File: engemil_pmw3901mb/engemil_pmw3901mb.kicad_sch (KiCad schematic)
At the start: 16 parts, among them J1 6130XX11121, U1 PMW3901MB-TXQT, U2 TLV77333PDBVR, U3 TLV77318PDBVR

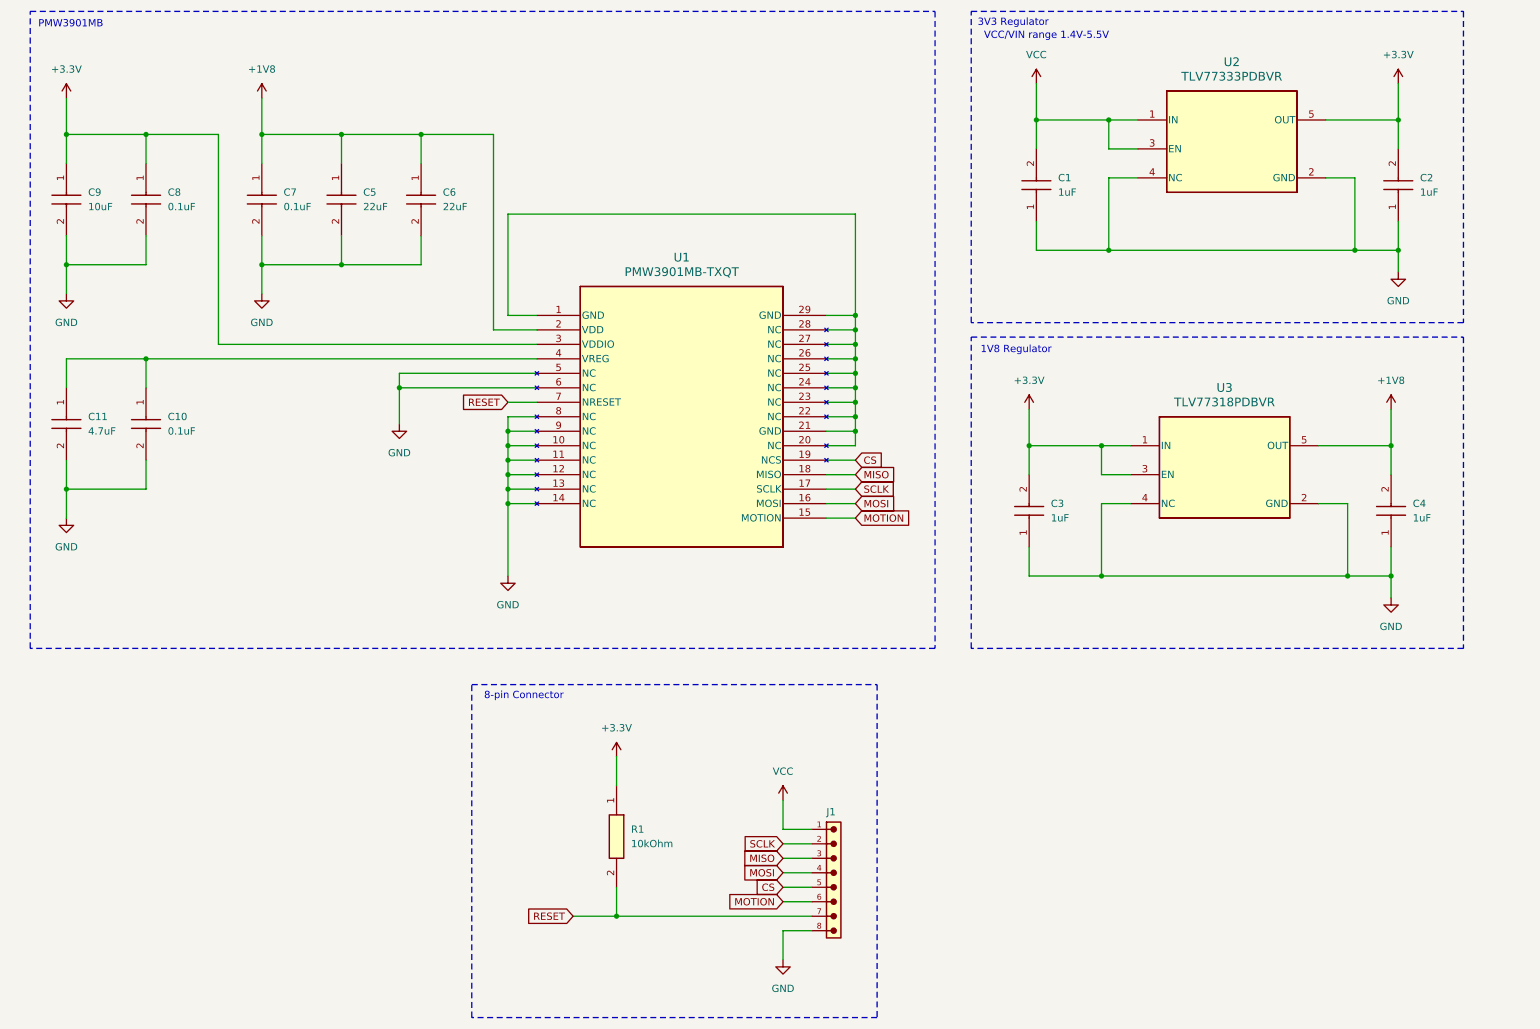
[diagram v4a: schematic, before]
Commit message: - Updated notes in schematic - Updated PMW3901MB NCS pin fron not connected to unspecified - Updated component orientation in PCB editor
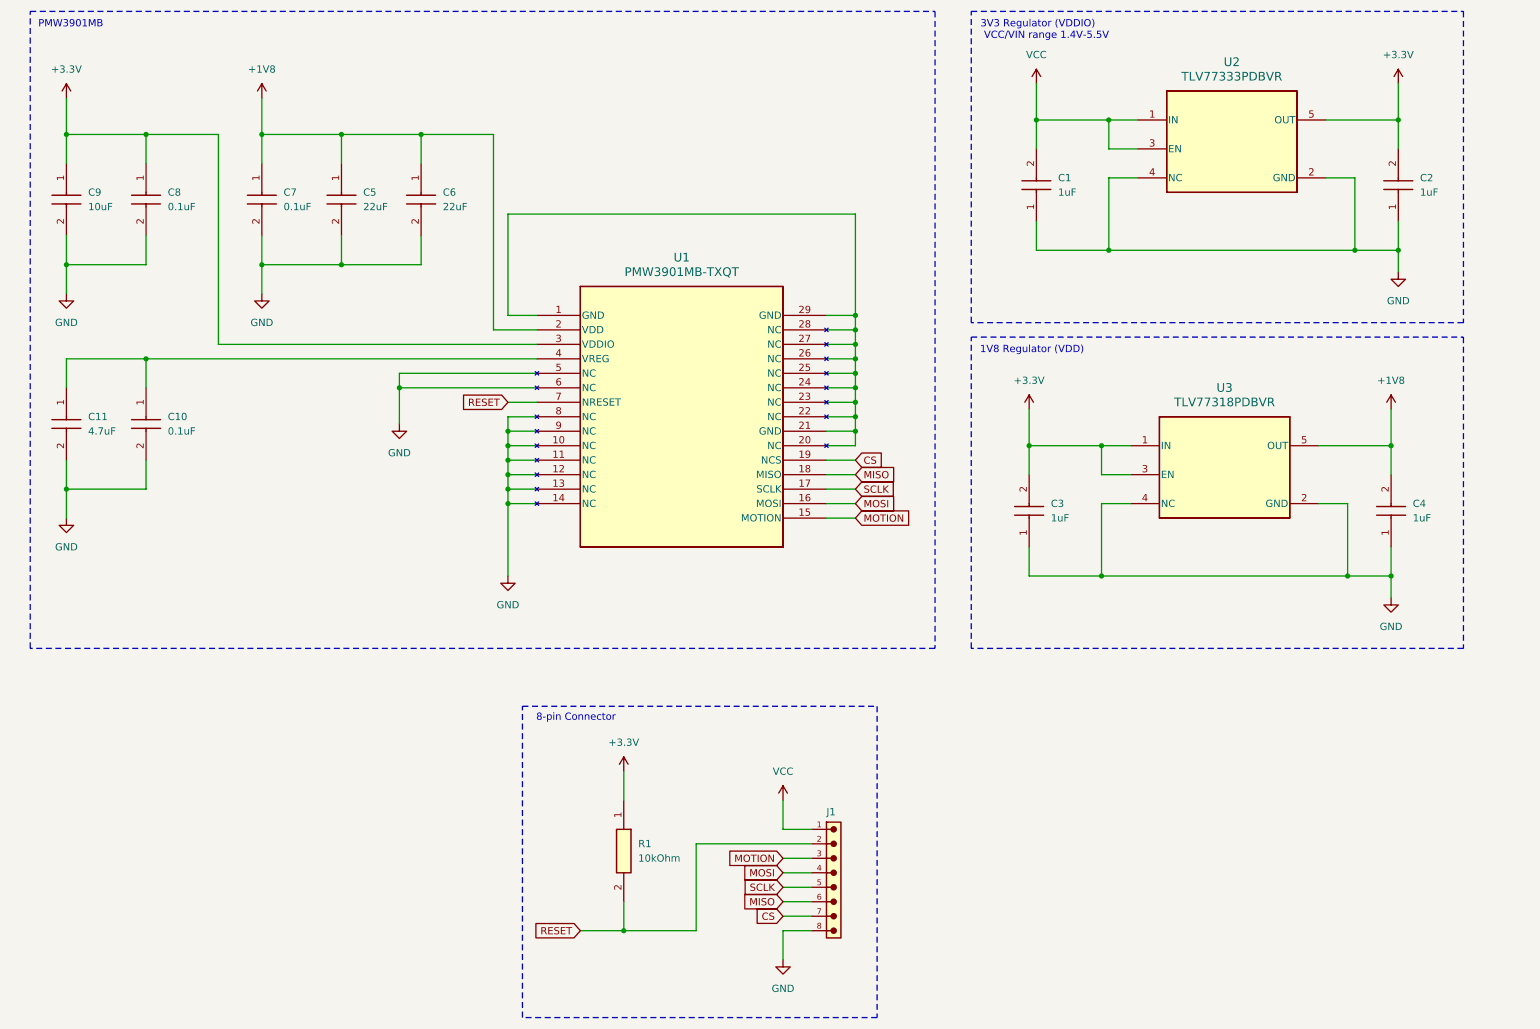
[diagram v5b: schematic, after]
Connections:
- net CS: now also J1.7; no longer J1.5
- net MISO: now also J1.6; no longer J1.3
- net MOTION: now also J1.3; no longer J1.6
- net RESET: now also J1.2; no longer J1.7
- net SCLK: now also J1.5; no longer J1.2
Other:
- note added: "1V8 Regulator (VDD)"
- note added: "3V3 Regulator (VDDIO)"
- note removed: "1V8 Regulator"
- note removed: "3V3 Regulator"
- moved on the sheet: R1
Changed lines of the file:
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@@
 	)
 	(rectangle
-		(start 95.25 134.62)
+		(start 104.14 138.43)
 		(end 166.37 193.04)
 		(stroke
@@
 	(text "8-pin Connector"
 		(exclude_from_sim no)
-		(at 104.394 136.652 0)
+		(at 113.538 140.462 0)
 		(effects
 			(font
@@
 		)
 	)
-	(text "3V3 Regulator"
+	(text "3V3 Regulator (VDDIO)"
 		(exclude_from_sim no)
-		(at 190.246 18.542 0)
+		(at 194.564 18.796 0)
 		(effects
 			(font
@@
 		)
 	)
-	(text "1V8 Regulator"
+	(text "1V8 Regulator (VDD)"
 		(exclude_from_sim no)
-		(at 190.754 75.946 0)
+		(at 193.548 75.946 0)
 		(effects
 			(font
@@
 	)
 	(junction
-		(at 120.65 175.26)
-		(diameter 0)
-		(color 0 0 0 0)
-	)
-	(junction
 		(at 193.04 92.71)
 		(diameter 0)
@@
 	)
 	(junction
+		(at 121.92 177.8)
+		(diameter 0)
+		(color 0 0 0 0)
+	)
+	(junction
 		(at 162.56 69.85)
 		(diameter 0)
@@
 	(wire
 		(pts
+			(xy 149.86 172.72) (xy 154.94 172.72)
+		)
+		(stroke
+			(width 0)
+			(type default)
+		)
+	)
+	(wire
+		(pts
 			(xy 205.74 115.57) (xy 193.04 115.57)
 		)
@@
 	(wire
 		(pts
-			(xy 243.84 102.87) (xy 248.92 102.87)
+			(xy 149.86 175.26) (xy 154.94 175.26)
 		)
 		(stroke
@@
 	(wire
 		(pts
-			(xy 149.86 172.72) (xy 154.94 172.72)
+			(xy 243.84 102.87) (xy 248.92 102.87)
 		)
 		(stroke
@@
 	(wire
 		(pts
-			(xy 149.86 170.18) (xy 154.94 170.18)
+			(xy 86.36 55.88) (xy 86.36 60.96)
 		)
 		(stroke
@@
 	(wire
 		(pts
-			(xy 86.36 55.88) (xy 86.36 60.96)
+			(xy 134.62 177.8) (xy 121.92 177.8)
 		)
 		(stroke
@@
 	(wire
 		(pts
-			(xy 120.65 175.26) (xy 154.94 175.26)
+			(xy 194.31 35.56) (xy 194.31 40.64)
 		)
 		(stroke
@@
 	(wire
 		(pts
-			(xy 194.31 35.56) (xy 194.31 40.64)
+			(xy 72.39 60.96) (xy 72.39 55.88)
 		)
 		(stroke
@@
 	(wire
 		(pts
-			(xy 72.39 60.96) (xy 72.39 55.88)
+			(xy 24.13 38.1) (xy 24.13 43.18)
 		)
 		(stroke
@@
 	(wire
 		(pts
-			(xy 24.13 38.1) (xy 24.13 43.18)
+			(xy 101.6 85.09) (xy 106.68 85.09)
 		)
 		(stroke
@@
 	(wire
 		(pts
-			(xy 101.6 85.09) (xy 106.68 85.09)
+			(xy 149.86 170.18) (xy 154.94 170.18)
 		)
 		(stroke
@@
 	(wire
 		(pts
-			(xy 162.56 82.55) (xy 162.56 85.09)
+			(xy 134.62 162.56) (xy 134.62 177.8)
 		)
 		(stroke
@@
 	(wire
 		(pts
-			(xy 257.81 58.42) (xy 257.81 62.23)
+			(xy 162.56 82.55) (xy 162.56 85.09)
 		)
 		(stroke
@@
 	(wire
 		(pts
-			(xy 212.09 40.64) (xy 207.01 40.64)
+			(xy 257.81 58.42) (xy 257.81 62.23)
 		)
 		(stroke
@@
 	(wire
 		(pts
-			(xy 149.86 162.56) (xy 154.94 162.56)
+			(xy 212.09 40.64) (xy 207.01 40.64)
 		)
 		(stroke
@@
 	(wire
 		(pts
-			(xy 113.03 175.26) (xy 120.65 175.26)
+			(xy 114.3 177.8) (xy 121.92 177.8)
+		)
+		(stroke
+			(width 0)
+			(type default)
+		)
+	)
+	(wire
+		(pts
+			(xy 154.94 162.56) (xy 134.62 162.56)
 		)
 		(stroke
@@
 	(wire
 		(pts
-			(xy 120.65 170.18) (xy 120.65 175.26)
+			(xy 121.92 172.72) (xy 121.92 177.8)
 		)
 		(stroke
@@
 	(wire
 		(pts
+			(xy 149.86 165.1) (xy 154.94 165.1)
+		)
+		(stroke
+			(width 0)
+			(type default)
+		)
+	)
+	(wire
+		(pts
 			(xy 101.6 102.87) (xy 106.68 102.87)
 		)
@@
 	(wire
 		(pts
-			(xy 120.65 147.32) (xy 120.65 152.4)
+			(xy 121.92 149.86) (xy 121.92 154.94)
 		)
 		(stroke
@@
 	(wire
 		(pts
-			(xy 149.86 165.1) (xy 154.94 165.1)
+			(xy 149.86 167.64) (xy 154.94 167.64)
 		)
 		(stroke
@@
 	(wire
 		(pts
-			(xy 149.86 167.64) (xy 154.94 167.64)
-		)
-		(stroke
-			(width 0)
-			(type default)
-		)
-	)
-	(wire
-		(pts
 			(xy 24.13 100.33) (xy 24.13 95.25)
 		)
@@
 	(global_label "MOTION"
 		(shape input)
-		(at 149.86 172.72 180)
+		(at 149.86 165.1 180)
 		(fields_autoplaced yes)
 		(effects
@@
 		)
 		(property "Intersheetrefs" "${INTERSHEET_REFS}"
-			(at 139.8595 172.72 0)
+			(at 139.8595 165.1 0)
 			(effects
 				(font
@@
 	(global_label "MISO"
 		(shape input)
-		(at 149.86 165.1 180)
+		(at 149.86 172.72 180)
 		(fields_autoplaced yes)
 		(effects
@@
 		)
 		(property "Intersheetrefs" "${INTERSHEET_REFS}"
-			(at 142.2786 165.1 0)
+			(at 142.2786 172.72 0)
 			(effects
 				(font
@@
 	(global_label "SCLK"
 		(shape input)
-		(at 149.86 162.56 180)
+		(at 149.86 170.18 180)
 		(fields_autoplaced yes)
 		(effects
@@
 		)
 		(property "Intersheetrefs" "${INTERSHEET_REFS}"
-			(at 142.0972 162.56 0)
+			(at 142.0972 170.18 0)
 			(effects
 				(font
@@
 	(global_label "RESET"
 		(shape input)
-		(at 113.03 175.26 180)
+		(at 114.3 177.8 180)
 		(fields_autoplaced yes)
 		(effects
@@
 		)
 		(property "Intersheetrefs" "${INTERSHEET_REFS}"
-			(at 104.2997 175.26 0)
+			(at 105.5697 177.8 0)
 			(effects
 				(font
@@
 	(global_label "CS"
 		(shape input)
-		(at 149.86 170.18 180)
+		(at 149.86 175.26 180)
 		(fields_autoplaced yes)
 		(effects
@@
 		)
 		(property "Intersheetrefs" "${INTERSHEET_REFS}"
-			(at 144.3953 170.18 0)
+			(at 144.3953 175.26 0)
 			(effects
 				(font
@@
 	(symbol
 		(lib_id "power:+3.3V")
-		(at 120.65 147.32 0)
+		(at 121.92 149.86 0)
 		(unit 1)
 		(exclude_from_sim no)
@@
 		(dnp no)
 		(property "Reference" "#PWR015"
-			(at 120.65 151.13 0)
+			(at 121.92 153.67 0)
 			(effects
 				(font
@@
 		)
 		(property "Value" "+3.3V"
-			(at 120.65 142.24 0)
+			(at 121.92 144.78 0)
 			(effects
 				(font
@@
 		)
 		(property "Footprint" ""
-			(at 120.65 147.32 0)
+			(at 121.92 149.86 0)
 			(effects
 				(font
@@
 		)
 		(property "Datasheet" ""
-			(at 120.65 147.32 0)
+			(at 121.92 149.86 0)
 			(effects
 				(font
@@
 		)
 		(property "Description" "Power symbol creates a global label with name \"+3.3V\""
-			(at 120.65 147.32 0)
+			(at 121.92 149.86 0)
 			(effects
 				(font
@@
 	(symbol
 		(lib_id "engemil_pmw3901mb_module_symbol_library:RE0805FRE0710KL")
-		(at 120.65 152.4 270)
+		(at 121.92 154.94 270)
 		(unit 1)
 		(exclude_from_sim no)
@@
 		(fields_autoplaced yes)
 		(property "Reference" "R1"
-			(at 123.19 160.0199 90)
+			(at 124.46 162.5599 90)
 			(effects
 				(font
@@
 		)
 		(property "Value" "10kOhm"
-			(at 123.19 162.5599 90)
+			(at 124.46 165.0999 90)
 			(effects
 				(font
@@
 		)
 		(property "Footprint" "RESC2012X60N"
-			(at 24.46 166.37 0)
+			(at 25.73 168.91 0)
 			(effects
 				(font
@@
 		)
 		(property "Datasheet" "https://www.yageo.com/upload/media/product/app/datasheet/rchip/pyu-re_105_rohs_l.pdf"
-			(at -75.54 166.37 0)
+			(at -74.27 168.91 0)
 			(effects
 				(font
@@
 		)
 		(property "Description" ""
-			(at 117.348 152.654 0)
+			(at 118.618 155.194 0)
 			(effects
 				(font
@@
 		)
 		(property "Height" "0.6"
-			(at -275.54 166.37 0)
+			(at -274.27 168.91 0)
 			(effects
 				(font
@@
 		)
 		(property "Mouser Part Number" "603-RE0805FRE0710KL"
-			(at -375.54 166.37 0)
+			(at -374.27 168.91 0)
 			(effects
 				(font
@@
 		)
 		(property "Mouser Price/Stock" "https://www.mouser.co.uk/ProductDetail/YAGEO/RE0805FRE0710KL?qs=HEu%2FF%2FCqxzLXGIUQzS%252BC%252BA%3D%3D"
-			(at -475.54 166.37 0)
+			(at -474.27 168.91 0)
 			(effects
 				(font
@@
 		)
 		(property "Manufacturer_Name" "YAGEO"
-			(at -575.54 166.37 0)
+			(at -574.27 168.91 0)
 			(effects
 				(font
@@
 		)
 		(property "Manufacturer_Part_Number" "RE0805FRE0710KL"
-			(at -675.54 166.37 0)
+			(at -674.27 168.91 0)
 			(effects
 				(font

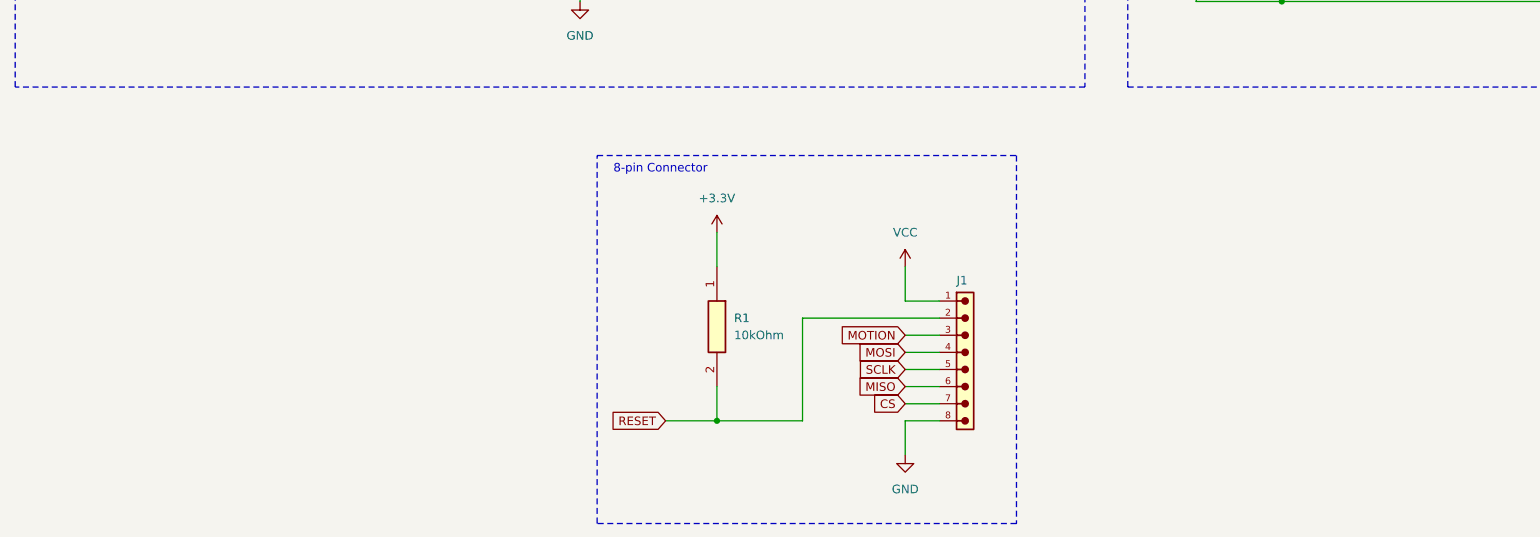
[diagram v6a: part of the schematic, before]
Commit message: - Added mounting holes in Schematic and PCB - Finished traces and top and bottom ground plains - Added vias for copper islands / isolated copper - Generated pdf of schematic and pcb - Updated README with 3D model
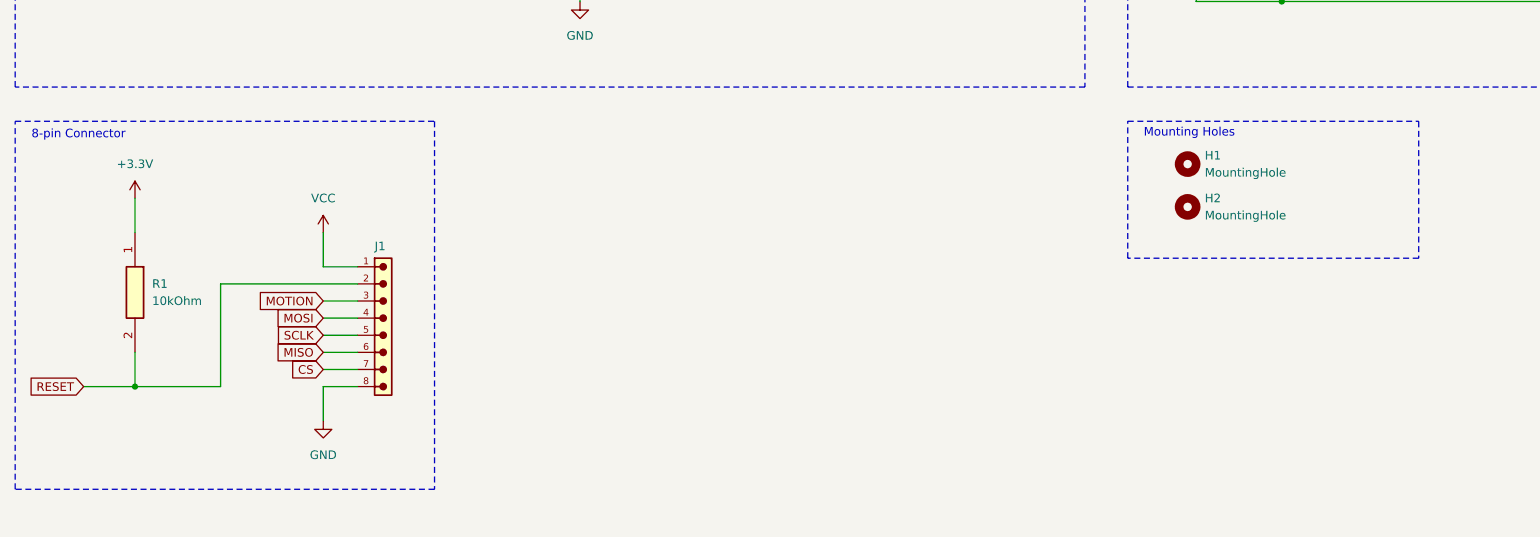
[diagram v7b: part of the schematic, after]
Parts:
- added H1, H2: MountingHole, MountingHole:MountingHole_3.2mm_M3_ISO14580, symbol Mechanical:MountingHole
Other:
- note added: "Mounting Holes"
- moved on the sheet: J1, R1
